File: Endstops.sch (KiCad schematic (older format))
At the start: 0 parts

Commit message: added endstop schematic
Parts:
- added C? (x9): 2.2uF, symbol Device:C_Small
- added D? (x9): LED, symbol Device:LED_Small
- added D? (x9): Schottky, symbol Device:D_Schottky_Small
- added J? (x9): Conn_01x03, symbol Connector_Generic:Conn_01x03
- added R? (x9): 2.2k, symbol Device:R_Small_US
- added R? (x9): 10k, symbol Device:R_Small_US
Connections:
- new net: D?.1 (K), J?.1 (Pin_1), R?.1 (x9)
- new net: D?.2 (A), R?.2 (x9)
- new net +3V3: D?.1 (K), D?.1 (K), D?.1 (K), D?.1 (K), D?.1 (K), D?.1 (K), D?.1 (K), D?.1 (K), D?.1 (K), J?.2 (Pin_2), J?.2 (Pin_2), J?.2 (Pin_2), J?.2 (Pin_2), J?.2 (Pin_2), J?.2 (Pin_2), J?.2 (Pin_2), J?.2 (Pin_2), J?.2 (Pin_2), R?.1, R?.1, R?.1, R?.1, R?.1, R?.1, R?.1, R?.1, R?.1
- new net E0_STOP: C?.1, D?.2 (A), R?.2
- new net E1_STOP: C?.1, D?.2 (A), R?.2
- new net E2_STOP: C?.1, D?.2 (A), R?.2
- new net E3_STOP: C?.1, D?.2 (A), R?.2
- new net E4_STOP: C?.1, D?.2 (A), R?.2
- new net E5_STOP: C?.1, D?.2 (A), R?.2
- new net GND: C?.2, C?.2, C?.2, C?.2, C?.2, C?.2, C?.2, C?.2, C?.2, J?.3 (Pin_3), J?.3 (Pin_3), J?.3 (Pin_3), J?.3 (Pin_3), J?.3 (Pin_3), J?.3 (Pin_3), J?.3 (Pin_3), J?.3 (Pin_3), J?.3 (Pin_3)
- new net X_STOP: C?.1, D?.2 (A), R?.2
- new net Y_STOP: C?.1, D?.2 (A), R?.2
- new net Z_STOP: C?.1, D?.2 (A), R?.2

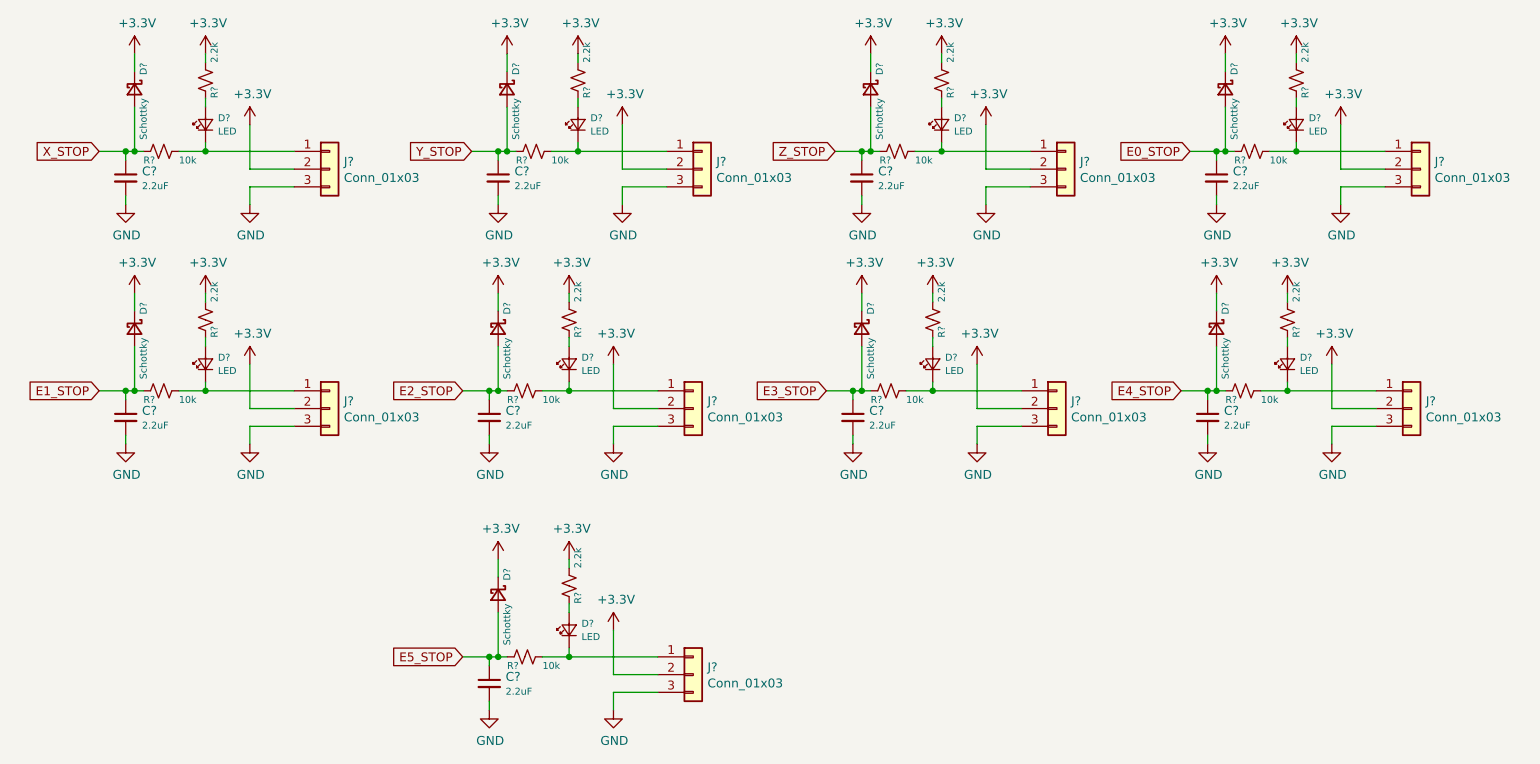
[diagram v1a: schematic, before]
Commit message: added raspberry pi header
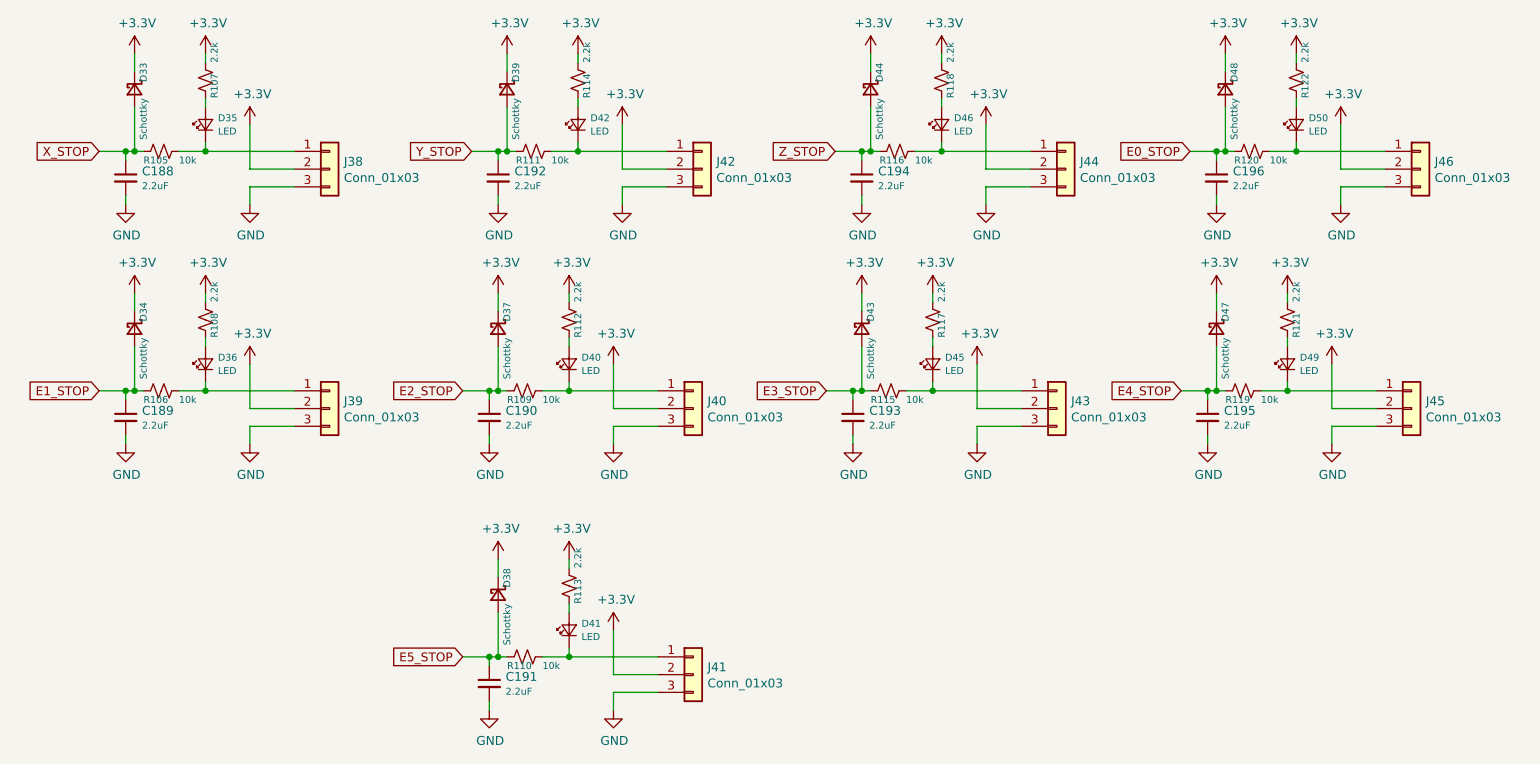
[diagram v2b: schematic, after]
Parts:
- gave numbers to parts that had none: 54

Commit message: associated more footprints
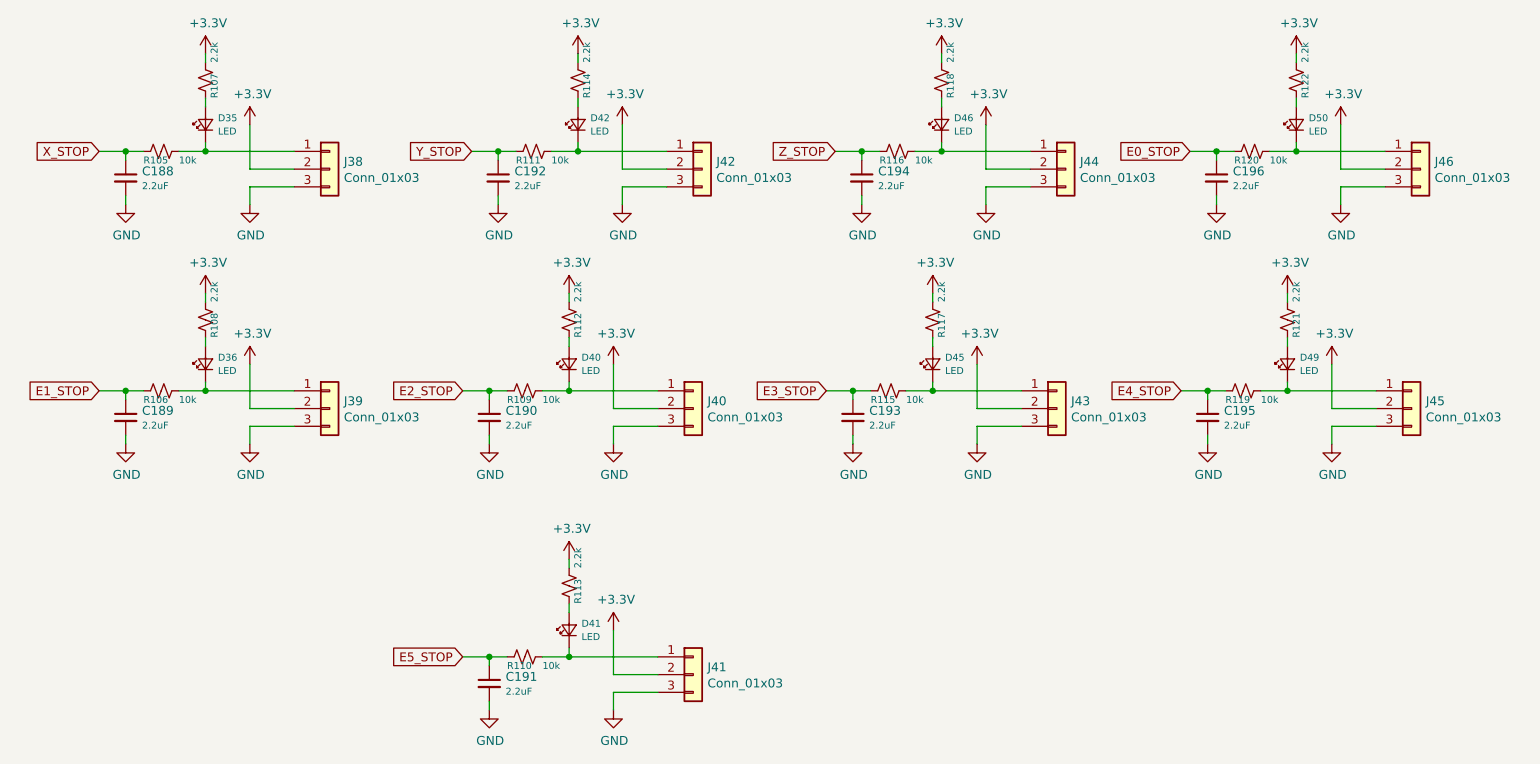
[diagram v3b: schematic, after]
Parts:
- removed D33, D34, D37, D38, D39, D43, D44, D47, D48: Schottky, symbol Device:D_Schottky_Small
- C188, C189, C190, C191, C192, C193, C194, C195, C196: footprint (none) -> Capacitor_SMD:C_0603_1608Metric_Pad1.05x0.95mm_HandSolder
- D35, D36, D40, D41, D42, D45, D46, D49, D50: footprint (none) -> LED_SMD:LED_0603_1608Metric_Pad1.05x0.95mm_HandSolder
- J38, J39, J40, J41, J42, J43, J44, J45, J46: footprint (none) -> Connector_Molex:Molex_KK-254_AE-6410-03A_1x03_P2.54mm_Vertical

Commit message: Added more footprints
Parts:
- R105, R106, R107, R108, R109, R110, R111, R112, R113, R114, R115, R116, R117, R118, R119, R120, R121, R122: footprint (none) -> Resistor_SMD:R_0603_1608Metric_Pad1.05x0.95mm_HandSolder
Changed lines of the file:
@@
 $Descr A4 11693 8268
 encoding utf-8
-Sheet 6 9
+Sheet 5 9
 Title ""
 Date "2020-10-23"
@@
 F 0 "R111" V 4600 1250 39  0000 L CNN
 F 1 "10k" V 4600 1450 39  0000 L CNN
-F 2 "" H 4550 1350 50  0001 C CNN
+F 2 "Resistor_SMD:R_0603_1608Metric_Pad1.05x0.95mm_HandSolder" H 4550 1350 50  0001 C CNN
 F 3 "~" H 4550 1350 50  0001 C CNN
 	1    4550 1350
@@
 F 0 "R114" V 4850 850 39  0000 L CNN
 F 1 "2.2k" V 4850 1050 39  0000 L CNN
-F 2 "" H 4800 950 50  0001 C CNN
+F 2 "Resistor_SMD:R_0603_1608Metric_Pad1.05x0.95mm_HandSolder" H 4800 950 50  0001 C CNN
 F 3 "~" H 4800 950 50  0001 C CNN
 	1    4800 950
@@
 F 0 "R105" V 2500 1250 39  0000 L CNN
 F 1 "10k" V 2500 1450 39  0000 L CNN
-F 2 "" H 2450 1350 50  0001 C CNN
+F 2 "Resistor_SMD:R_0603_1608Metric_Pad1.05x0.95mm_HandSolder" H 2450 1350 50  0001 C CNN
 F 3 "~" H 2450 1350 50  0001 C CNN
 	1    2450 1350
@@
 F 0 "R107" V 2750 850 39  0000 L CNN
 F 1 "2.2k" V 2750 1050 39  0000 L CNN
-F 2 "" H 2700 950 50  0001 C CNN
+F 2 "Resistor_SMD:R_0603_1608Metric_Pad1.05x0.95mm_HandSolder" H 2700 950 50  0001 C CNN
 F 3 "~" H 2700 950 50  0001 C CNN
 	1    2700 950
@@
 F 0 "R116" V 6650 1250 39  0000 L CNN
 F 1 "10k" V 6650 1450 39  0000 L CNN
-F 2 "" H 6600 1350 50  0001 C CNN
+F 2 "Resistor_SMD:R_0603_1608Metric_Pad1.05x0.95mm_HandSolder" H 6600 1350 50  0001 C CNN
 F 3 "~" H 6600 1350 50  0001 C CNN
 	1    6600 1350
@@
 F 0 "R118" V 6900 850 39  0000 L CNN
 F 1 "2.2k" V 6900 1050 39  0000 L CNN
-F 2 "" H 6850 950 50  0001 C CNN
+F 2 "Resistor_SMD:R_0603_1608Metric_Pad1.05x0.95mm_HandSolder" H 6850 950 50  0001 C CNN
 F 3 "~" H 6850 950 50  0001 C CNN
 	1    6850 950
@@
 F 0 "R120" V 8650 1250 39  0000 L CNN
 F 1 "10k" V 8650 1450 39  0000 L CNN
-F 2 "" H 8600 1350 50  0001 C CNN
+F 2 "Resistor_SMD:R_0603_1608Metric_Pad1.05x0.95mm_HandSolder" H 8600 1350 50  0001 C CNN
 F 3 "~" H 8600 1350 50  0001 C CNN
 	1    8600 1350
@@
 F 0 "R122" V 8900 850 39  0000 L CNN
 F 1 "2.2k" V 8900 1050 39  0000 L CNN
-F 2 "" H 8850 950 50  0001 C CNN
+F 2 "Resistor_SMD:R_0603_1608Metric_Pad1.05x0.95mm_HandSolder" H 8850 950 50  0001 C CNN
 F 3 "~" H 8850 950 50  0001 C CNN
 	1    8850 950
@@
 F 0 "R106" V 2500 2600 39  0000 L CNN
 F 1 "10k" V 2500 2800 39  0000 L CNN
-F 2 "" H 2450 2700 50  0001 C CNN
+F 2 "Resistor_SMD:R_0603_1608Metric_Pad1.05x0.95mm_HandSolder" H 2450 2700 50  0001 C CNN
 F 3 "~" H 2450 2700 50  0001 C CNN
 	1    2450 2700
@@
 F 0 "R108" V 2750 2200 39  0000 L CNN
 F 1 "2.2k" V 2750 2400 39  0000 L CNN
-F 2 "" H 2700 2300 50  0001 C CNN
+F 2 "Resistor_SMD:R_0603_1608Metric_Pad1.05x0.95mm_HandSolder" H 2700 2300 50  0001 C CNN
 F 3 "~" H 2700 2300 50  0001 C CNN
 	1    2700 2300
@@
 F 0 "R109" V 4550 2600 39  0000 L CNN
 F 1 "10k" V 4550 2800 39  0000 L CNN
-F 2 "" H 4500 2700 50  0001 C CNN
+F 2 "Resistor_SMD:R_0603_1608Metric_Pad1.05x0.95mm_HandSolder" H 4500 2700 50  0001 C CNN
 F 3 "~" H 4500 2700 50  0001 C CNN
 	1    4500 2700
@@
 F 0 "R112" V 4800 2200 39  0000 L CNN
 F 1 "2.2k" V 4800 2400 39  0000 L CNN
-F 2 "" H 4750 2300 50  0001 C CNN
+F 2 "Resistor_SMD:R_0603_1608Metric_Pad1.05x0.95mm_HandSolder" H 4750 2300 50  0001 C CNN
 F 3 "~" H 4750 2300 50  0001 C CNN
 	1    4750 2300
@@
 F 0 "R115" V 6600 2600 39  0000 L CNN
 F 1 "10k" V 6600 2800 39  0000 L CNN
-F 2 "" H 6550 2700 50  0001 C CNN
+F 2 "Resistor_SMD:R_0603_1608Metric_Pad1.05x0.95mm_HandSolder" H 6550 2700 50  0001 C CNN
 F 3 "~" H 6550 2700 50  0001 C CNN
 	1    6550 2700
@@
 F 0 "R117" V 6850 2200 39  0000 L CNN
 F 1 "2.2k" V 6850 2400 39  0000 L CNN
-F 2 "" H 6800 2300 50  0001 C CNN
+F 2 "Resistor_SMD:R_0603_1608Metric_Pad1.05x0.95mm_HandSolder" H 6800 2300 50  0001 C CNN
 F 3 "~" H 6800 2300 50  0001 C CNN
 	1    6800 2300
@@
 F 0 "R119" V 8600 2600 39  0000 L CNN
 F 1 "10k" V 8600 2800 39  0000 L CNN
-F 2 "" H 8550 2700 50  0001 C CNN
+F 2 "Resistor_SMD:R_0603_1608Metric_Pad1.05x0.95mm_HandSolder" H 8550 2700 50  0001 C CNN
 F 3 "~" H 8550 2700 50  0001 C CNN
 	1    8550 2700
@@
 F 0 "R121" V 8850 2200 39  0000 L CNN
 F 1 "2.2k" V 8850 2400 39  0000 L CNN
-F 2 "" H 8800 2300 50  0001 C CNN
+F 2 "Resistor_SMD:R_0603_1608Metric_Pad1.05x0.95mm_HandSolder" H 8800 2300 50  0001 C CNN
 F 3 "~" H 8800 2300 50  0001 C CNN
 	1    8800 2300
@@
 F 0 "R110" V 4550 4100 39  0000 L CNN
 F 1 "10k" V 4550 4300 39  0000 L CNN
-F 2 "" H 4500 4200 50  0001 C CNN
+F 2 "Resistor_SMD:R_0603_1608Metric_Pad1.05x0.95mm_HandSolder" H 4500 4200 50  0001 C CNN
 F 3 "~" H 4500 4200 50  0001 C CNN
 	1    4500 4200
@@
 F 0 "R113" V 4800 3700 39  0000 L CNN
 F 1 "2.2k" V 4800 3900 39  0000 L CNN
-F 2 "" H 4750 3800 50  0001 C CNN
+F 2 "Resistor_SMD:R_0603_1608Metric_Pad1.05x0.95mm_HandSolder" H 4750 3800 50  0001 C CNN
 F 3 "~" H 4750 3800 50  0001 C CNN
 	1    4750 3800
